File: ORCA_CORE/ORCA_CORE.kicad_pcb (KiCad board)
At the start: 4 copper layers, 73 x 134.1 mm, 184 parts, among them J1 data_line_power, J10 Raspberry_Pi_2_3, J11 I2C, J12 I2C, J13 6Vout, J15 Conn_01x05_Pin, J16 Conn_01x05_Pin, J17 Vin_motor, J18 data_line_power, J19 +5Vin_cpu, J2 I2C_power, J20 5Vout, J21 Conn_01x02, J3 Vout_motor, J4 emergence, J5 Vin_batt, J6 Vin_ex, J7 Vout_power2usp, J8 Vin_power2usp, J9 +5Vout_cpu, P1 USB_C_Receptacle_USB2.0, Q1 TJ60S04M3L, Q2 BSS138, Q3 BSS138, Q4 IRLML6402, Q5 TJ60S04M3L, Q6 BSS138, Q7 BSS138, Q8 BSS138, U1 LTC2301IMS, U10 HY2112, U11 AP64502, U12 TPS61230A__board, U13 FT230XS, U14 BNO055, U15 NJM78055DL1, U2 NJM78055DL1, U3 CN3058E, U4 RH1B-UDC6V, U5 TPH11006NL, U6 TPH11006NL, U7 NJW4860, U8 AZ1117-3.3, U9 FS8205

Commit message: placed an order
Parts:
- J21: footprint Battery:BatteryHolder_1xAA_code -> battery_case:BatteryHolder_1xAA_code
- R19: value 10 -> 360
- U12: footprint Converter_DCDC:TPS61230A -> converter_module:TPS61230A
- U4: footprint Relay_THT:RH1-U -> relay:RH1-U
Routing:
- net GND2: vias 49 -> 48

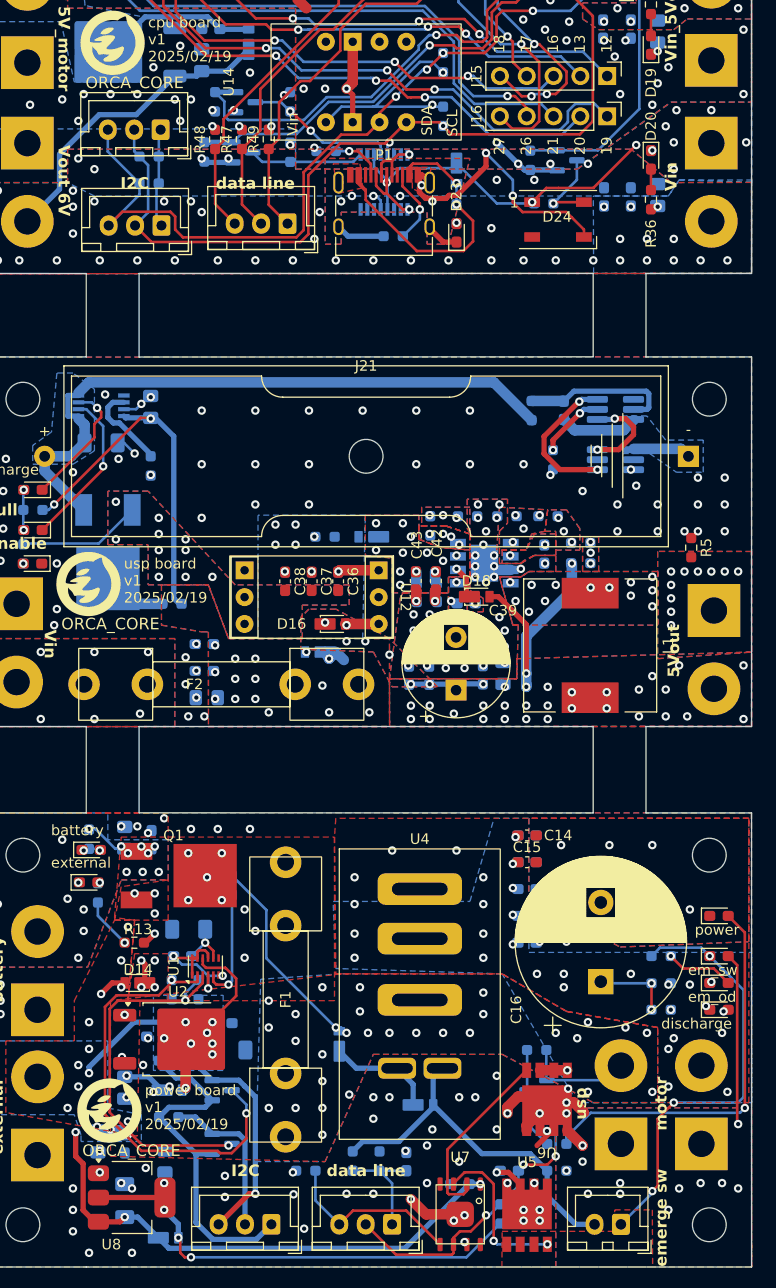
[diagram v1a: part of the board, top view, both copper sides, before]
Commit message: delete blind vias
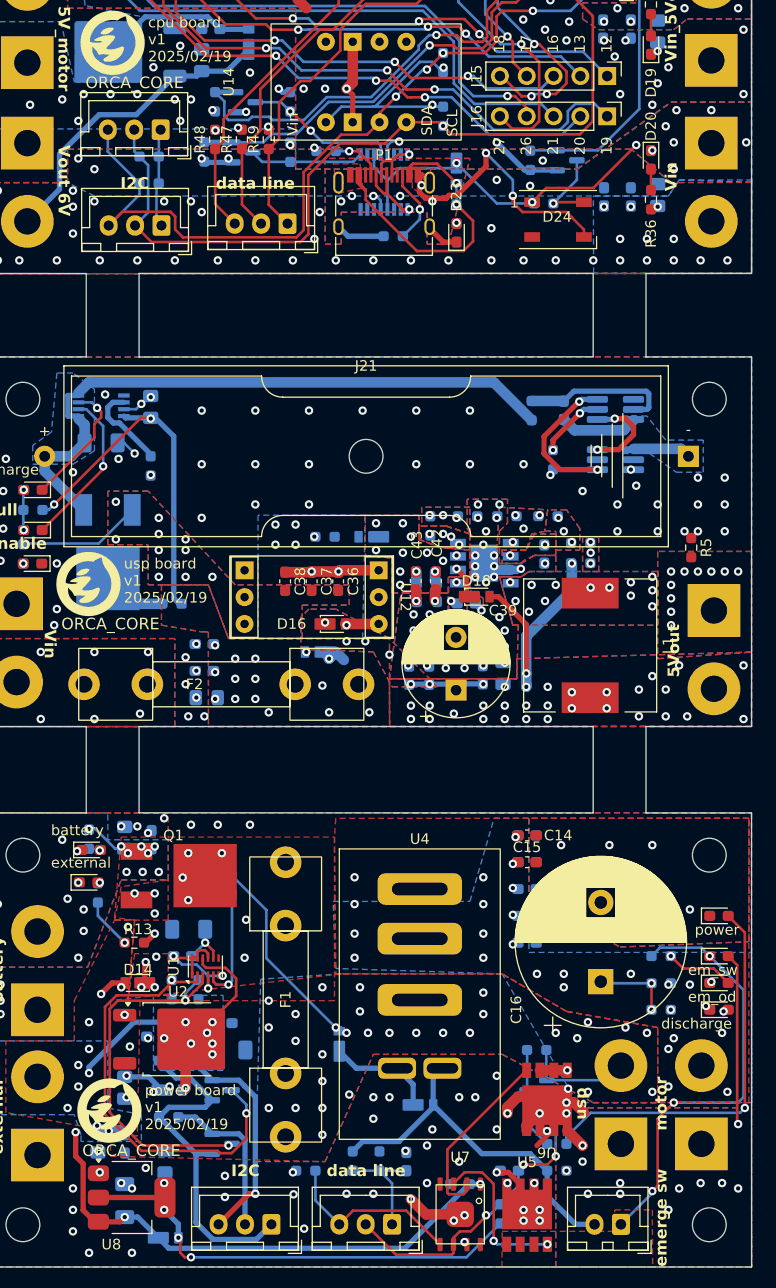
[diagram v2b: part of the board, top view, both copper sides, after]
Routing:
- net +5V_cpu: track 57.6 -> 64.6 mm
- net GND: track 73.9 -> 79.0 mm, vias 211 -> 206
- net Net-(U11-SW): track 4.14 -> 5.44 mm
- net +3V3_cpu: track 61.8 -> 62.8 mm
- net GND2: track 146.4 -> 147.3 mm
- net Net-(Q1-G): vias 6 -> 5
- net /power/Vout_motor: vias 27 -> 25
- net +VDD_power: vias 14 -> 12
- net +6V_cpu: vias 46 -> 44

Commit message: made board outline and import it
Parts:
- removed C13, C14, C15, C18, C22, C26, C28, C31, C32, C36, C37, C38, C40, C41, C42, C43, C46, C47, C51: 4.7u, Capacitor_SMD:C_0603_1608Metric_Pad1.08x0.95mm_HandSolder
- removed C16: 4700u, Capacitor_THT:CP_Radial_D16.0mm_P7.50mm
- removed C17, C30, C34, C35, C45: 0.1u, Capacitor_SMD:C_0603_1608Metric_Pad1.08x0.95mm_HandSolder
- removed C19: 10u/50V, Capacitor_SMD:C_1206_3216Metric_Pad1.33x1.80mm_HandSolder
- removed C20: 22u25V, Capacitor_SMD:C_0805_2012Metric_Pad1.18x1.45mm_HandSolder
- removed C21, C23, C24, C27, C33, C44, C48: 1u, Capacitor_SMD:C_0805_2012Metric_Pad1.18x1.45mm_HandSolder
- removed C25: 10u, Capacitor_SMD:C_1206_3216Metric_Pad1.33x1.80mm_HandSolder
- removed C29: 0.01u, Capacitor_SMD:C_0603_1608Metric_Pad1.08x0.95mm_HandSolder
- removed C39: 1000u, Capacitor_THT:CP_Radial_D10.0mm_P5.00mm
- removed C49: 1u/50V, Capacitor_SMD:C_0805_2012Metric_Pad1.18x1.45mm_HandSolder
- removed C50: 0.1u25V, Capacitor_SMD:C_0603_1608Metric_Pad1.08x0.95mm_HandSolder
- removed D10: LED_charge, LED_SMD:LED_0603_1608Metric_Pad1.05x0.95mm_HandSolder
- removed D11, D13, D14, D16, D17, D18, D22, D25, D9: CUHS20560, Diode:Diode_US2H
- removed D12: LED_full, LED_SMD:LED_0603_1608Metric_Pad1.05x0.95mm_HandSolder
- removed D15: LED_batt_enabled, LED_SMD:LED_0603_1608Metric_Pad1.05x0.95mm_HandSolder
- removed D20: LED_motor, LED_SMD:LED_0603_1608Metric_Pad1.05x0.95mm_HandSolder
- removed D23: LED_usb, LED_SMD:LED_0603_1608Metric_Pad1.05x0.95mm_HandSolder
- removed D24: WS2812B, LED_SMD:LED_WS2812B_PLCC4_5.0x5.0mm_P3.2mm
- removed F1, F2: Fuse, fuse:fuse
- removed L1: 10u, inductor:L_12x12mm_H8mm_withmodel
- removed ORCA_CORE (x3): LOGO, Logo:ORCA_logo
- removed Q4: IRLML6402, Package_TO_SOT_SMD:SOT-23
- removed Q5: TJ60S04M3L, toshiba:2-7M1A
- removed Q6, Q7: BSS138, Package_TO_SOT_SMD:SOT-23
- added H11: Hole_Vhub, MountingHole:MountingHole_3.2mm_M3, F.Cu at (-50.1, -137.2)
- added H12: Hole_Vhub, MountingHole:MountingHole_3.2mm_M3, F.Cu at (-42.1, -153.1)
- added H13: Hole_md, MountingHole:MountingHole_3.2mm_M3, F.Cu at (-92.0, 196.2)
- added H14: Hole_md, MountingHole:MountingHole_3.2mm_M3, F.Cu at (-92.0, 204.2)
- added H15: Hole_md, MountingHole:MountingHole_3.2mm_M3, F.Cu at (105.4, 71.9)
- added H16: Hole_md, MountingHole:MountingHole_3.2mm_M3, F.Cu at (105.4, 97.4)
- added H17: Hole_hat, MountingHole:MountingHole_3.2mm_M3, F.Cu at (162.0, -92.0)
- added H18: Hole_hat, MountingHole:MountingHole_3.2mm_M3, F.Cu at (162.0, -84.0)
- added H19: Hole_hat, MountingHole:MountingHole_3.2mm_M3, F.Cu at (162.0, -76.1)
- added H20: Hole_hat, MountingHole:MountingHole_3.2mm_M3, F.Cu at (162.0, -68.2)
- added H21: Hole_cpu, MountingHole:MountingHole_3.2mm_M3, F.Cu at (-307.2, -27.6)
- added H22: Hole_cup, MountingHole:MountingHole_3.2mm_M3, F.Cu at (-307.2, -19.7)
- added H23: Hole_usbA, MountingHole:MountingHole_3.2mm_M3, F.Cu at (-42.1, -145.2)
- added H24: Hole_usbA, MountingHole:MountingHole_3.2mm_M3, F.Cu at (-42.1, -137.2)
- added H7: Hole_Vext, MountingHole:MountingHole_3.2mm_M3, F.Cu at (-50.1, -153.1)
- added H8: Hole_Vext, MountingHole:MountingHole_3.2mm_M3, F.Cu at (-50.1, -145.2)
- added J14: limit_sw_upper, Connector_JST:JST_XH_S2B-XH-A_1x02_P2.50mm_Horizontal, F.Cu at (-87.4, 182.0)
- added J22: Vin_motor, Connector_JST:JST_XH_S2B-XH-A_1x02_P2.50mm_Horizontal, F.Cu at (127.0, 75.5)
- added J23: md_arm, Connector_JST:JST_XH_B6B-XH-A_1x06_P2.50mm_Vertical, F.Cu at (48.5, -92.6)
- added J24: md_fork, Connector_JST:JST_XH_B6B-XH-A_1x06_P2.50mm_Vertical, F.Cu at (48.5, -84.8)
- added J25: servo_arm, Connector_JST:JST_XH_B6B-XH-A_1x06_P2.50mm_Vertical, F.Cu at (48.5, -77.0)
- added J26: Vin_motor, Connector_JST:JST_XH_S2B-XH-A_1x02_P2.50mm_Horizontal, F.Cu at (-90.0, 1.64)
- added J27: servo_0, Connector_PinHeader_2.54mm:PinHeader_1x03_P2.54mm_Horizontal, F.Cu at (-114.2, -16.9)
- added J28: servo_1, Connector_PinHeader_2.54mm:PinHeader_1x03_P2.54mm_Horizontal, F.Cu at (-114.2, -7.23)
- added J29: servo_2, Connector_PinHeader_2.54mm:PinHeader_1x03_P2.54mm_Horizontal, F.Cu at (-114.2, 2.47)
- added J30: servo_3, Connector_PinHeader_2.54mm:PinHeader_1x03_P2.54mm_Horizontal, F.Cu at (-114.2, 12.2)
- added J31: I2C_1, Connector_JST:JST_XH_B3B-XH-A_1x03_P2.50mm_Vertical, F.Cu at (169.4, -84.8)
- added J32: I2C_2, Connector_JST:JST_XH_B3B-XH-A_1x03_P2.50mm_Vertical, F.Cu at (169.4, -77.0)
- added J33: cpu_male_2, Connector_PinHeader_2.54mm:PinHeader_2x05_P2.54mm_Vertical, F.Cu at (-305.4, -91.1)
- added J34: cpu_male_1, Connector_PinHeader_2.54mm:PinHeader_2x10_P2.54mm_Vertical, F.Cu at (-290.9, -118.2)
- added J35: hat_female_1, Connector_PinHeader_2.54mm:PinHeader_2x10_P2.54mm_Vertical, F.Cu at (88.5, -78.0)
- added J36: enable_arm, Connector_JST:JST_XH_S2B-XH-A_1x02_P2.50mm_Horizontal, F.Cu at (-134.0, -26.0)
- added J37: enable_arm, Connector_JST:JST_XH_B2B-XH-A_1x02_P2.50mm_Vertical, F.Cu at (82.4, -92.6)
- added J38: servo_arm, Connector_JST:JST_XH_S6B-XH-A_1x06_P2.50mm_Horizontal, F.Cu at (-144.0, -4.00)
- added J39: md_arm, Connector_JST:JST_XH_S6B-XH-A_1x06_P2.50mm_Horizontal, F.Cu at (110.5, 78.3)
- added J40: md_fork, Connector_JST:JST_XH_S6B-XH-A_1x06_P2.50mm_Horizontal, F.Cu at (-125.0, 187.0)
- added J41: cpu_female_2, Connector_PinHeader_2.54mm:PinHeader_2x05_P2.54mm_Vertical, F.Cu at (74.0, -51.0)
- added J42: uart, Connector_JST:JST_XH_B4B-XH-A_1x04_P2.50mm_Vertical, F.Cu at (68.0, -92.6)
- added J43: uart_device, Connector_JST:JST_XH_S4B-XH-A_1x04_P2.50mm_Horizontal, F.Cu at (-109.3, -138.2)
- added J44: servo_camera, Connector_PinHeader_2.54mm:PinHeader_1x03_P2.54mm_Vertical, F.Cu at (-282.0, -26.1)
- added J45: reset, Connector_JST:JST_XH_S3B-XH-A_1x03_P2.50mm_Horizontal, F.Cu at (-80.8, -110.7)
- added J46: reset, Connector_JST:JST_XH_B3B-XH-A_1x03_P2.50mm_Vertical, F.Cu at (96.8, -77.0)
- added J47: led, Connector_JST:JST_XH_B3B-XH-A_1x03_P2.50mm_Vertical, F.Cu at (96.8, -69.2)
- added J48: led, Connector_JST:JST_XH_B3B-XH-A_1x03_P2.50mm_Vertical, F.Cu at (-80.4, -122.5)
- added J49: USB_B_Micro, digikey-footprints:USB_Micro_B_Male_UJ2-MIBH-4-SMT-TR, F.Cu at (169.6, -67.6)
- added J50: USB_A, Connector_USB:USB_A_Kycon_KUSBX-AS1N-B_Horizontal, F.Cu at (-34.2, -130.7)
- added J51: usb_A_device, Connector_JST:JST_XH_S4B-XH-A_1x04_P2.50mm_Horizontal, F.Cu at (-109.3, -124.6)
- added J52: usb_A, Connector_JST:JST_XH_B4B-XH-A_1x04_P2.50mm_Vertical, F.Cu at (68.0, -84.8)
- added R52: 100, Resistor_SMD:R_0603_1608Metric_Pad0.98x0.95mm_HandSolder, F.Cu at (-304.7, -61.3)
- added R53: 2.2k, Resistor_SMD:R_0603_1608Metric_Pad0.98x0.95mm_HandSolder, F.Cu at (-304.7, -58.8)
- added R54: 2.2k, Resistor_SMD:R_0603_1608Metric_Pad0.98x0.95mm_HandSolder, F.Cu at (-304.7, -56.3)
- added R55: 100, Resistor_SMD:R_0603_1608Metric_Pad0.98x0.95mm_HandSolder, F.Cu at (-304.7, -53.8)
- added R56: 2.2k, Resistor_SMD:R_0603_1608Metric_Pad0.98x0.95mm_HandSolder, F.Cu at (-304.7, -51.3)
- added R57: 2.2k, Resistor_SMD:R_0603_1608Metric_Pad0.98x0.95mm_HandSolder, F.Cu at (180.1, -89.7)
- added R58: 2.2k, Resistor_SMD:R_0603_1608Metric_Pad0.98x0.95mm_HandSolder, F.Cu at (180.1, -87.2)
- added R59: 100, Resistor_SMD:R_0603_1608Metric_Pad0.98x0.95mm_HandSolder, F.Cu at (-304.7, -48.8)
- added R60: 2.2k, Resistor_SMD:R_0603_1608Metric_Pad0.98x0.95mm_HandSolder, F.Cu at (-300.4, -68.8)
- added R61: 2.2k, Resistor_SMD:R_0603_1608Metric_Pad0.98x0.95mm_HandSolder, F.Cu at (-300.4, -66.3)
- added R62: 100, Resistor_SMD:R_0603_1608Metric_Pad0.98x0.95mm_HandSolder, F.Cu at (-300.4, -63.8)
- added R63: 2.2k, Resistor_SMD:R_0603_1608Metric_Pad0.98x0.95mm_HandSolder, F.Cu at (-300.4, -61.3)
- added R64: 2.2k, Resistor_SMD:R_0603_1608Metric_Pad0.98x0.95mm_HandSolder, F.Cu at (-300.4, -58.8)
- added R65: 100, Resistor_SMD:R_0603_1608Metric_Pad0.98x0.95mm_HandSolder, F.Cu at (-300.4, -56.3)
- added R66: 2.2k, Resistor_SMD:R_0603_1608Metric_Pad0.98x0.95mm_HandSolder, F.Cu at (-300.4, -53.8)
- added R67: 2.2k, Resistor_SMD:R_0603_1608Metric_Pad0.98x0.95mm_HandSolder, F.Cu at (-300.4, -51.3)
- added R68: 100, Resistor_SMD:R_0603_1608Metric_Pad0.98x0.95mm_HandSolder, F.Cu at (-300.4, -48.8)
- added R69: 2.2k, Resistor_SMD:R_0603_1608Metric_Pad0.98x0.95mm_HandSolder, F.Cu at (-296.0, -68.8)
- added R70: 2.2k, Resistor_SMD:R_0603_1608Metric_Pad0.98x0.95mm_HandSolder, F.Cu at (-296.0, -66.3)
- added R71: 2.2k, Resistor_SMD:R_0603_1608Metric_Pad0.98x0.95mm_HandSolder, F.Cu at (-296.0, -63.8)
- added R72: 2.2k, Resistor_SMD:R_0603_1608Metric_Pad0.98x0.95mm_HandSolder, F.Cu at (-296.0, -61.3)
- added R73: 2.2k, Resistor_SMD:R_0603_1608Metric_Pad0.98x0.95mm_HandSolder, F.Cu at (-296.0, -58.8)
- added SW2: REST_sw, Button_Switch_THT:SW_PUSH_6mm, F.Cu at (-36.1, -145.1)
- added U16: TLP293, Package_SO:SOIC-4_4.55x2.6mm_P1.27mm, F.Cu at (-98.3, 17.0)
- added U17: AZ1117-3.3, Package_TO_SOT_SMD:SOT-223-3_TabPin2, F.Cu at (-88.5, 16.1)
- added U18: TLP293, Package_SO:SOIC-4_4.55x2.6mm_P1.27mm, F.Cu at (-298.4, -45.4)
- added U19: TLP293, Package_SO:SOIC-4_4.55x2.6mm_P1.27mm, F.Cu at (-298.4, -41.3)
- added U20: TLP293, Package_SO:SOIC-4_4.55x2.6mm_P1.27mm, F.Cu at (-298.4, -37.1)
- added U21: TLP293, Package_SO:SOIC-4_4.55x2.6mm_P1.27mm, F.Cu at (-298.4, -33.0)
- added U22: AZ1117-3.3, Package_TO_SOT_SMD:SOT-223-3_TabPin2, F.Cu at (-277.6, -56.2)
- added U23: TLP293, Package_SO:SOIC-4_4.55x2.6mm_P1.27mm, F.Cu at (-298.4, -28.8)
- added U24: TLP293, Package_SO:SOIC-4_4.55x2.6mm_P1.27mm, F.Cu at (-298.4, -24.7)
- added U25: TLP293, Package_SO:SOIC-4_4.55x2.6mm_P1.27mm, F.Cu at (-298.4, -20.5)
- C1: value 1u/50V -> 10u/50V; footprint Capacitor_SMD:C_0805_2012Metric_Pad1.18x1.45mm_HandSolder -> Capacitor_SMD:C_1206_3216Metric_Pad1.33x1.80mm_HandSolder; moved to F.Cu
- C10, C12: value 4.7u -> 22u25V; footprint Capacitor_SMD:C_0603_1608Metric_Pad1.08x0.95mm_HandSolder -> Capacitor_SMD:C_0805_2012Metric_Pad1.18x1.45mm_HandSolder; moved to F.Cu
- C11, C9: value 4.7u -> 10u/50V; footprint Capacitor_SMD:C_0603_1608Metric_Pad1.08x0.95mm_HandSolder -> Capacitor_SMD:C_1206_3216Metric_Pad1.33x1.80mm_HandSolder; moved to F.Cu
- C2: value 0.1u25V -> 22u25V; footprint Capacitor_SMD:C_0603_1608Metric_Pad1.08x0.95mm_HandSolder -> Capacitor_SMD:C_0805_2012Metric_Pad1.18x1.45mm_HandSolder; moved to F.Cu
- C3: value 0.1u -> 10u/50V; footprint Capacitor_SMD:C_0603_1608Metric_Pad1.08x0.95mm_HandSolder -> Capacitor_SMD:C_1206_3216Metric_Pad1.33x1.80mm_HandSolder
- C4: value 4.7u -> 22u25V; footprint Capacitor_SMD:C_0603_1608Metric_Pad1.08x0.95mm_HandSolder -> Capacitor_SMD:C_0805_2012Metric_Pad1.18x1.45mm_HandSolder
- C5: value 10u -> 0.1u; footprint Capacitor_SMD:C_1206_3216Metric_Pad1.33x1.80mm_HandSolder -> Capacitor_SMD:C_0603_1608Metric_Pad1.08x0.95mm_HandSolder; moved to F.Cu
- C6, Q2, Q8, R12, R34, R37, R38, R41, R43, R44, R46, R50, R6, R7, R8: moved to F.Cu
- C7: value 10u -> 220u; moved to F.Cu
- C8: value 0.1u -> 220u; footprint Capacitor_SMD:C_0603_1608Metric_Pad1.08x0.95mm_HandSolder -> Capacitor_SMD:C_1206_3216Metric_Pad1.33x1.80mm_HandSolder; moved to F.Cu
- D1: value LED_batt -> CUHS20560; footprint LED_SMD:LED_0603_1608Metric_Pad1.05x0.95mm_HandSolder -> Diode:Diode_US2H
- D19: value LED_cpu -> pwr_cpu
- D2: value LED_ex -> CUHS20560; footprint LED_SMD:LED_0603_1608Metric_Pad1.05x0.95mm_HandSolder -> Diode:Diode_US2H; moved to B.Cu
- D3: value CUHS20560 -> WS2812B; footprint Diode:Diode_US2H -> LED_SMD:LED_WS2812B_PLCC4_5.0x5.0mm_P3.2mm; moved to F.Cu
- D4: value CUHS20560 -> enable_arm; footprint Diode:Diode_US2H -> LED_SMD:LED_0603_1608Metric_Pad1.05x0.95mm_HandSolder; moved to F.Cu
- D5: value LED_power -> power_input_arm
- D6: value LED_emerge_switch -> CUHS20560; footprint LED_SMD:LED_0603_1608Metric_Pad1.05x0.95mm_HandSolder -> Diode:Diode_US2H
- D7: value LED_emerge_order -> CUHS20560; footprint LED_SMD:LED_0603_1608Metric_Pad1.05x0.95mm_HandSolder -> Diode:Diode_US2H
- D8: value LED_discharge -> pwr_motor
- H1, H2: value Hole_power -> Hole_uart
- H3, H4: value Hole_power -> Hole_led
- H5, H6: value Hole_usp -> Hole_reset
- J1: value data_line_power -> Vext_in; footprint Connector_JST:JST_XH_B3B-XH-A_1x03_P2.50mm_Vertical -> Conn:AMASS_XT60_Vertifcal_withmodel_female
- J11: value I2C -> wheel_left; footprint Connector_JST:JST_XH_B3B-XH-A_1x03_P2.50mm_Vertical -> Connector_PinHeader_2.54mm:PinHeader_1x03_P2.54mm_Vertical
- J12: value I2C -> md_out; footprint Connector_JST:JST_XH_B3B-XH-A_1x03_P2.50mm_Vertical -> Connector_JST:JST_XH_S2B-XH-A_1x02_P2.50mm_Horizontal
- J13: value 6Vout -> md_out; footprint Conn:power_pad -> Connector_JST:JST_XH_S2B-XH-A_1x02_P2.50mm_Horizontal
- J15: value Conn_01x05_Pin -> limit_sw_upper; footprint Connector_PinHeader_2.54mm:PinHeader_1x05_P2.54mm_Vertical -> Connector_JST:JST_XH_S2B-XH-A_1x02_P2.50mm_Horizontal
- J16: value Conn_01x05_Pin -> limit_sw_under; footprint Connector_PinHeader_2.54mm:PinHeader_1x05_P2.54mm_Vertical -> Connector_JST:JST_XH_S2B-XH-A_1x02_P2.50mm_Horizontal
- J17: value Vin_motor -> data_line_power; footprint Conn:power_pad -> Connector_JST:JST_XH_B3B-XH-A_1x03_P2.50mm_Vertical
- J18: value data_line_power -> +6V_motor; footprint Connector_JST:JST_XH_B3B-XH-A_1x03_P2.50mm_Vertical -> Conn:power_pad
- J2: value I2C_power -> 6Vout; footprint Connector_JST:JST_XH_B3B-XH-A_1x03_P2.50mm_Vertical -> Conn:AMASS_XT30U-F_Vertical_withmodel_male
- J20: value 5Vout -> limit_sw_under; footprint Conn:power_pad -> Connector_JST:JST_XH_S2B-XH-A_1x02_P2.50mm_Horizontal
- J21: value Conn_01x02 -> Vin_motor; footprint battery_case:BatteryHolder_1xAA_code -> Connector_JST:JST_XH_S2B-XH-A_1x02_P2.50mm_Horizontal
- J3: value Vout_motor -> 6Vout; footprint Conn:power_pad -> Conn:AMASS_XT30U-F_Vertical_withmodel_male
- J4: value emergence -> 6Vout; footprint Connector_JST:JST_XH_B2B-XH-A_1x02_P2.50mm_Vertical -> Conn:AMASS_XT30U-F_Vertical_withmodel_male
- J5: value Vin_batt -> 6Vin; footprint Conn:power_pad -> Conn:AMASS_XT60_Vertifcal_withmodel_female
- J6: value Vin_ex -> Vext_out
- J7: value Vout_power2usp -> 6Vout; footprint Conn:power_pad -> Conn:AMASS_XT30U-F_Vertical_withmodel_male
- J8: value Vin_power2usp -> wheel_front; footprint Conn:power_pad -> Connector_PinHeader_2.54mm:PinHeader_1x03_P2.54mm_Horizontal
- J9: value +5Vout_cpu -> wheel_right; footprint Conn:power_pad -> Connector_PinHeader_2.54mm:PinHeader_1x03_P2.54mm_Vertical
- Q1: value TJ60S04M3L -> BSS138; footprint toshiba:2-7M1A -> Package_TO_SOT_SMD:SOT-23
- Q3: value BSS138 -> TJ60S04M3L; footprint Package_TO_SOT_SMD:SOT-23 -> toshiba:2-7M1A; moved to F.Cu
- R1: value 1k -> 560; moved to F.Cu
- R10, R42, R45: value 2.2k -> 100; moved to F.Cu
- R11: value 2.2k -> 100
- R13: value 4.7k -> 2.2k; moved to B.Cu
- R14, R17, R18, R20, R22, R40: value 1k -> 2.2k; moved to F.Cu
- R15, R4: value 4.7k -> 2.2k; moved to F.Cu
- R16: value 4.7k -> 100; moved to F.Cu
- R19: value 360 -> 100
- R2: value 1k -> 5.1k; moved to F.Cu
- R21: value 1.2k -> 2.2k
- R23: value 100k -> 2.2k
- R24: value 100k -> 2.2k; moved to F.Cu
- R25: value 47k -> 2.2k
- R26: value 4.7k -> 10k; moved to F.Cu
- R27: value 510 -> 1k; moved to F.Cu
- R28: value 10k -> 1k; moved to F.Cu
- R29: value 2k -> 100; moved to F.Cu
- R3: value 4.7k -> 5.1k; moved to F.Cu
- R30: value 100 -> 2.2k; moved to F.Cu
- R31: value 1k -> 47; moved to F.Cu
- R32: value 10k -> 100; moved to F.Cu
- R33: value 10k -> 2.2k; moved to F.Cu
- R36: value 1k -> 2.2k
- R39, R51: value 5.1k -> 100; moved to F.Cu
- R49: value 2.2k -> 1k
- R5: value 0 -> 2.2k
- R9: value 2.2k -> 10k; moved to F.Cu
- U1: value LTC2301IMS -> FT230XS; footprint Package_DFN_QFN:TDFN-12_2x3mm_P0.5mm -> Package_SO:SSOP-16_3.9x4.9mm_P0.635mm
- U10: value HY2112 -> TLP293; footprint Package_TO_SOT_SMD:TSOT-23-6_HandSoldering -> Package_SO:SOIC-4_4.55x2.6mm_P1.27mm; moved to F.Cu
- U11: value AP64502 -> TLP293; footprint Package_SO:Diodes_SO-8EP -> Package_SO:SOIC-4_4.55x2.6mm_P1.27mm; moved to F.Cu
- U12: value TPS61230A__board -> TLP293; footprint converter_module:TPS61230A -> Package_SO:SOIC-4_4.55x2.6mm_P1.27mm
- U13: value FT230XS -> TLP293; footprint Package_SO:SSOP-16_3.9x4.9mm_P0.635mm -> Package_SO:SOIC-4_4.55x2.6mm_P1.27mm; moved to F.Cu
- U15: value NJM78055DL1 -> TLP293; footprint Package_TO_SOT_SMD:TO-252-2 -> Package_SO:SOIC-4_4.55x2.6mm_P1.27mm; moved to F.Cu
- U2: value NJM78055DL1 -> PCA9685PW_Q900_118; footprint Package_TO_SOT_SMD:TO-252-2 -> digikey-footprints:TSSOP-28_W4.40mm
- U3: value CN3058E -> AM2837; footprint Package_SO:TSSOP-8_3x3mm_P0.65mm -> Package_SO:SOP-8_3.9x4.9mm_P1.27mm; moved to F.Cu
- U4: value RH1B-UDC6V -> AM2837; footprint relay:RH1-U -> Package_SO:SOP-8_3.9x4.9mm_P1.27mm; moved to B.Cu
- U5, U6: value TPH11006NL -> TLP293; footprint toshiba:2-5Q1S -> Package_SO:SOIC-4_4.55x2.6mm_P1.27mm
- U7: value NJW4860 -> AZ1117-3.3; footprint nisshinbo:TSOP8-M1 -> Package_TO_SOT_SMD:SOT-223-3_TabPin2
- U8: moved to B.Cu
- U9: value FS8205 -> TLP293; footprint Package_TO_SOT_SMD:TSOT-23-6_HandSoldering -> Package_SO:SOIC-4_4.55x2.6mm_P1.27mm; moved to F.Cu
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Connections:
- net full_color_led_5V renamed /cpu/led
- C1 pad 1: +6V_power -> +6V
- C10 pad 1: /power/Vout_motor -> +3V3
- C11 pad 1: /power/Vout_motor -> +6V
- C12 pad 1: /power/Vout_motor -> +3V3_motor
- C2 pad 1: +5V_power -> +3V3
- C3 pad 1: /power/power_checker -> +6V
- C4 pad 1: GND -> +3V3
- C4 pad 2: +VDD_power -> GND
- C5 pad 1: GND -> +6V
- C5 pad 2: Net-(U1-REFCOMP) -> GND
- C6 pad 1: GND -> +6V
- C6 pad 2: Net-(U1-REFCOMP) -> GND
- C7 pad 1: +5V_power -> +6V
- C8 pad 1: +5V_power -> +6V
- C9 pad 1: /power/Vout_motor -> +6V_in
- D1 pad 1: GND -> +6V
- D1 pad 2: Net-(D1-A) -> +3V3
- D19 pad 1: GND2 -> GND1
- D2 pad 1: GND -> +6V
- D2 pad 2: Net-(D2-A) -> +3V3
- D3 pad 1: Net-(D3-K) -> /external_io/+5V_led
- D3 pad 2: +6V_power -> unconnected-(D3-DOUT-Pad2)
- D4 pad 1: Net-(D3-K) -> GND
- D6 pad 1: Net-(D6-K) -> +6V_in
- D6 pad 2: Net-(D6-A) -> +3V3
- D7 pad 1: GND -> +6V
- D7 pad 2: Net-(D7-A) -> +3V3_motor
- D8 pad 1: Net-(D8-K) -> GND
- J1 pad 1: /power/emerg_detector -> Net-(J1-Pin_1)
- J1 pad 2: /power/power_checker -> Net-(J1-Pin_2)
- J10 pad 1: +3V3_cpu -> +3V3
- J10 pad 13: /cpu/GPIO27 -> unconnected-(J10-GPIO27-Pad13)
- J10 pad 14: GND2 -> GND1
- J10 pad 15: /cpu/emerg_detector -> emerge_detector
- J10 pad 16: /cpu/emerge_order -> power_checker
- J10 pad 17: +3V3_cpu -> +3V3
- J10 pad 18: /cpu/power_checker -> emerge_order
- J10 pad 2: +5V_cpu -> +5V
- J10 pad 20: GND2 -> GND1
- J10 pad 25: GND2 -> GND1
- J10 pad 3: SDA -> /cpu/SDA_cpu
- J10 pad 30: GND2 -> GND1
- J10 pad 34: GND2 -> GND1
- J10 pad 35: /cpu/GPIO19 -> /cpu/rest
- J10 pad 37: /cpu/GPIO26 -> unconnected-(J10-GPIO26-Pad37)
- J10 pad 38: /cpu/GPIO20 -> unconnected-(J10-GPIO20/MOSI1-Pad38)
- J10 pad 39: GND2 -> GND1
- J10 pad 4: +5V_cpu -> +5V
- J10 pad 40: /cpu/GPIO21 -> unconnected-(J10-GPIO21/SCLK1-Pad40)
- J10 pad 5: SCL -> /cpu/SCL_cpu
- J10 pad 6: GND2 -> GND1
- J10 pad 9: GND2 -> GND1
- J11 pad 1: +3V3_cpu -> GND
- J11 pad 2: SCL -> +6V
- J11 pad 3: SDA -> Net-(J11-Pin_3)
- J12 pad 1: +3V3_cpu -> Net-(J12-Pin_1)
- J12 pad 2: SCL -> Net-(J12-Pin_2)
- J13 pad 1: GND -> Net-(J13-Pin_1)
- J13 pad 2: +6V_cpu -> Net-(J13-Pin_2)
- J15 pad 1: /cpu/GPIO12 -> GND1
- J15 pad 2: /cpu/GPIO13 -> /md_arm/limit_sw_upper
- J16 pad 1: /cpu/GPIO19 -> GND1
- J16 pad 2: /cpu/GPIO20 -> /md_fork/limit_sw_under
- J17 pad 1: GND -> /cpu_hat/emerge_detector
- J17 pad 2: +6V_cpu -> /cpu_hat/power_checker
- J18 pad 1: /cpu/emerg_detector -> GND
- J18 pad 2: /cpu/power_checker -> +6V
- J19 pad 1: GND2 -> GND1
- J19 pad 2: +5V_cpu -> +5V
- J2 pad 1: VBUS_power -> Net-(J2-Pin_1)
- J2 pad 2: /power/SCL_3V3 -> Net-(J2-Pin_2)
- J20 pad 1: GND -> GND1
- J20 pad 2: +5V_cpu2servo -> /md_arm/limit_sw_under
- J21 pad 1: batt- -> GND
- J21 pad 2: batt+ -> +6V
- J3 pad 1: GND -> Net-(J2-Pin_1)
- J3 pad 2: /power/Vout_motor -> Net-(J2-Pin_2)
- J4 pad 1: Net-(D6-K) -> Net-(J2-Pin_1)
- J4 pad 2: Net-(D4-A) -> Net-(J2-Pin_2)
- J5 pad 1: GND -> Net-(J2-Pin_1)
- J5 pad 2: +BATT_power -> Net-(J2-Pin_2)
- J6 pad 1: GND -> Net-(J1-Pin_1)
- J6 pad 2: +VDD_power -> Net-(J1-Pin_2)
- J7 pad 1: GND -> Net-(J2-Pin_1)
- J7 pad 2: +6V_power -> Net-(J2-Pin_2)
- J8 pad 2: /usp/Vin -> +6V
- J9 pad 1: GND1 -> GND
- J9 pad 2: reg_down_out -> +6V
- P1 pad A1: GND2 -> /external_io/GND_uart
- P1 pad A12: GND2 -> /external_io/GND_uart
- P1 pad A4: Net-(D22-A) -> /external_io/+5V_uart
- P1 pad A6: Net-(U13-USBDP) -> Net-(U1-USBDP)
- P1 pad A7: Net-(U13-USBDM) -> Net-(U1-USBDM)
- P1 pad A9: Net-(D22-A) -> /external_io/+5V_uart
- P1 pad B1: GND2 -> /external_io/GND_uart
- P1 pad B12: GND2 -> /external_io/GND_uart
- P1 pad B4: Net-(D22-A) -> /external_io/+5V_uart
- P1 pad B6: Net-(U13-USBDP) -> Net-(U1-USBDP)
- P1 pad B7: Net-(U13-USBDM) -> Net-(U1-USBDM)
- P1 pad B9: Net-(D22-A) -> /external_io/+5V_uart
- P1 pad S1: GND2 -> /external_io/GND_uart
- Q1 pad 1: +BATT_power -> +3V3
- Q1 pad 2: Net-(Q1-G) -> TXD_3V3
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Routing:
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- removed copper zone on In1.Cu, net +3V3_cpu
- removed copper zone on B.Cu, net +5V_cpu
- removed copper zone on F.Cu, net +5V_cpu
- removed copper zone on In1.Cu, net +5V_cpu
- removed copper zone on In2.Cu, net +5V_cpu
- removed copper zone on B.Cu, net +5V_cpu2servo
- removed copper zone on In1.Cu, net +5V_cpu2servo
- removed copper zone on B.Cu, net +5V_power
- removed copper zone on B.Cu, net +6V_cpu
- removed copper zone on F.Cu, net +6V_cpu
- removed copper zone on In1.Cu, net +6V_cpu
- removed copper zone on B.Cu, net +6V_power
- removed copper zone on F.Cu, net +6V_power
- removed copper zone on In1.Cu, net +6V_power
- removed copper zone on B.Cu, net +BATT_power
- removed copper zone on F.Cu, net +BATT_power
- removed copper zone on In1.Cu, net +BATT_power
- removed copper zone on B.Cu, net +VDD_power
- removed copper zone on F.Cu, net +VDD_power
- removed copper zone on In1.Cu, net +VDD_power
- removed copper zone on B.Cu, net +VDD_usp
- removed copper zone on F.Cu, net +VDD_usp
- removed copper zone on In1.Cu, net +VDD_usp
- removed copper zone on B.Cu, net /power/Vout_motor
- removed copper zone on F.Cu, net /power/Vout_motor
- removed copper zone on In1.Cu, net /power/Vout_motor
- removed copper zone on B.Cu, net /usp/Vin
- removed copper zone on F.Cu, net /usp/Vin
- removed copper zone on In1.Cu, net /usp/Vin
- removed copper zone on In2.Cu, net /usp/Vin
- removed copper zone on In1.Cu, net GND
- removed copper zone on In2.Cu, net GND
- removed copper zone on In1.Cu, net GND1
- removed copper zone on In2.Cu, net GND1
- removed copper zone on B.Cu, net GND2
- removed copper zone on F.Cu, net GND2
- removed copper zone on In2.Cu, net GND2
- removed copper zone on F.Cu, net Net-(D14-K)
- removed copper zone on In1.Cu, net Net-(D14-K)
- removed copper zone on F.Cu, net Net-(D6-K)
- removed copper zone on In2.Cu, net Net-(Q1-G)
- removed copper zone on B.Cu, net Net-(R23-Pad2)
- removed copper zone on F.Cu, net Net-(R23-Pad2)
- removed copper zone on In1.Cu, net Net-(R23-Pad2)
- removed copper zone on In2.Cu, net Net-(R23-Pad2)
- removed copper zone on B.Cu, net Net-(R25-Pad1)
- removed copper zone on F.Cu, net Net-(R25-Pad1)
- removed copper zone on In1.Cu, net Net-(R25-Pad1)
- removed copper zone on In2.Cu, net Net-(R25-Pad1)
- removed copper zone on B.Cu, net Net-(R26-Pad2)
- removed copper zone on F.Cu, net Net-(R26-Pad2)
- removed copper zone on In1.Cu, net Net-(R26-Pad2)
- removed copper zone on In2.Cu, net Net-(R26-Pad2)
- removed copper zone on B.Cu, net Net-(U11-BST)
- removed copper zone on F.Cu, net Net-(U11-BST)
- removed copper zone on In1.Cu, net Net-(U11-BST)
- removed copper zone on In2.Cu, net Net-(U11-BST)
- removed copper zone on B.Cu, net Net-(U11-FB)
- removed copper zone on F.Cu, net Net-(U11-FB)
- removed copper zone on In1.Cu, net Net-(U11-FB)
- removed copper zone on In2.Cu, net Net-(U11-FB)
- removed copper zone on B.Cu, net Net-(U11-RT/CLK)
- removed copper zone on F.Cu, net Net-(U11-RT/CLK)
- removed copper zone on In1.Cu, net Net-(U11-RT/CLK)
- removed copper zone on In2.Cu, net Net-(U11-RT/CLK)
- removed copper zone on B.Cu, net Net-(U11-SS)
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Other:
- board size 73 x 134.1 mm -> 123.1 x 120.2 mm
- copper layers 4 -> 2
- board text removed: "12"
- board text removed: "13"
- board text removed: "16"
- board text removed: "17"
- board text removed: "18"
- board text removed: "19"
- board text removed: "20"
- board text removed: "21"
- board text removed: "26"
- board text removed: "27"
- board text removed: "3V3"
- board text removed: "5Vout"
- board text removed: "I2C"
- board text removed: "SCL"
- board text removed: "SDA"
- board text removed: "Vin"
- board text removed: "Vin_5Vcpu"
- board text removed: "Vout 5V_motor"
- board text removed: "Vout 6V"
- board text removed: "battery"
- board text removed: "charge"
- board text removed: "cpu board v1 2025/02/19"
- board text removed: "data line"
- board text removed: "discharge"
- board text removed: "em_od"
- board text removed: "em_sw"
- board text removed: "emerge sw"
- board text removed: "emerge_detector"
- board text removed: "emerge_order"
- board text removed: "enable"
- board text removed: "external"
- board text removed: "full"
- board text removed: "motor"
- board text removed: "power"
- board text removed: "power board v1 2025/02/19"
- board text removed: "power_checker"
- board text removed: "usp"
- board text removed: "usp board v1 2025/02/19"

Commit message: place most of footprints. test replicate
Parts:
- removed R57, R58: 2.2k, Resistor_SMD:R_0603_1608Metric_Pad0.98x0.95mm_HandSolder
- added J53: cover_left, Connector_PinHeader_2.54mm:PinHeader_1x07_P2.54mm_Vertical, B.Cu at (173.7, 139.7)
- added J54: base_left, Connector_PinSocket_2.54mm:PinSocket_1x07_P2.54mm_Vertical, F.Cu at (147.5, 76.2)
- added J59: base_right, Connector_PinSocket_2.54mm:PinSocket_2x10_P2.54mm_Vertical, F.Cu at (52.5, 89.8)
- added J60: cover_right, Connector_PinHeader_2.54mm:PinHeader_2x10_P2.54mm_Vertical, B.Cu at (209.3, 139.7)
- J10: footprint cpu:raspberrypi_Zero_W_Vertical -> cpu:raspberrypi_Zerp_W_horisontal
- J27, J28, J29, J30: footprint Connector_PinHeader_2.54mm:PinHeader_1x03_P2.54mm_Horizontal -> Connector_PinHeader_2.54mm:PinHeader_1x03_P2.54mm_Vertical
- J33: value cpu_male_2 -> cpu_female_left; footprint Connector_PinHeader_2.54mm:PinHeader_2x05_P2.54mm_Vertical -> Connector_PinSocket_2.54mm:PinSocket_2x05_P2.54mm_Vertical
- J34: value cpu_male_1 -> cpu_female_right; footprint Connector_PinHeader_2.54mm:PinHeader_2x10_P2.54mm_Vertical -> Connector_PinSocket_2.54mm:PinSocket_2x10_P2.54mm_Vertical
- J35: value hat_female_1 -> hat_male_right; moved to B.Cu
- J41: value cpu_female_2 -> cpu_male_left; moved to B.Cu
- J44, J9: footprint Connector_PinHeader_2.54mm:PinHeader_1x03_P2.54mm_Vertical -> Connector_PinHeader_2.54mm:PinHeader_1x03_P2.54mm_Horizontal
- J45: footprint Connector_JST:JST_XH_S3B-XH-A_1x03_P2.50mm_Horizontal -> Connector_JST:JST_XH_B3B-XH-A_1x03_P2.50mm_Vertical; moved to B.Cu
- J48, Q1, Q2, R1, R2, R3, R37, R38, R4, R5, R7, R8, U1, U18, U19, U20: moved to B.Cu
- J49: footprint digikey-footprints:USB_Micro_B_Male_UJ2-MIBH-4-SMT-TR -> Conn:ZX60-B-5S(31); moved to B.Cu
- U14: footprint IMU:BNO055 -> IMU:BNO055_short
- moved J10 497.5 mm to (114.0, 132.9), turned to 180 degrees
- moved R34 470.1 mm to (139.7, 86.4), turned to 90 degrees
- moved R6 470.0 mm to (135.0, 90.2)
- moved J33 464.2 mm to (130.2, 69.3), turned to 30 degrees
- moved R69 458.5 mm to (133.1, 92.7)
- moved R48 455.2 mm to (108.3, 122.6), turned to 180 degrees
- moved R68 452.4 mm to (127.8, 97.3), turned to 60 degrees
- moved J18 451.0 mm to (103.8, 136.9)
- moved R70 450.0 mm to (123.7, 96.1), turned to -30 degrees
- moved R55 449.8 mm to (108.3, 124.5)
- moved R56 447.4 mm to (108.2, 120.9), turned to 180 degrees
- moved R51 447.0 mm to (100.7, 124.5)
- moved R9 446.4 mm to (106.1, 108.0)
- moved D7 445.2 mm to (106.7, 157.9)
- moved R53 443.3 mm to (100.6, 120.9), turned to 180 degrees
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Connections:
- J17 pad 1: /cpu_hat/emerge_detector -> Net-(J17-Pin_1)
- J17 pad 2: /cpu_hat/power_checker -> Net-(J17-Pin_2)
- J17 pad 3: /cpu_hat/emerge_order -> Net-(J17-Pin_3)
- J23 pad 2: /cpu_hat/IN_A_fork -> /cpu_hat/IN_A_arm_out
- J23 pad 3: /cpu_hat/IN_B_fork -> /cpu_hat/IN_B_arm_out
- J23 pad 4: /cpu_hat/limit_sw_upper_arm -> /cpu_hat/limit_sw_upper_arm_in
- J23 pad 5: /cpu_hat/limit_sw_under_arm -> /cpu_hat/limit_sw_under_arm_in
- J24 pad 2: /cpu_hat/IN_A_arm -> /cpu_hat/IN_A_fork_out
- J24 pad 3: /cpu_hat/IN_B_arm -> /cpu_hat/IN_B_fork_out
- J24 pad 4: /cpu_hat/limit_sw_upper_fork -> /cpu_hat/limit_sw_upper_fork_in
- J24 pad 5: /cpu_hat/limit_sw_under_fork -> /cpu_hat/limit_sw_under_fork_in
- J25 pad 2: /cpu_hat/servo_0 -> /cpu_hat/servo_0_out
- J25 pad 3: /cpu_hat/servo_1 -> /cpu_hat/servo_1_out
- J25 pad 4: /cpu_hat/servo_2 -> /cpu_hat/servo_2_out
- J25 pad 5: /cpu_hat/servo_3 -> /cpu_hat/servo_3_out
- J31 pad 2: /cpu_hat/SCL -> Net-(J31-Pin_2)
- J31 pad 3: /cpu_hat/SDA -> Net-(J31-Pin_3)
- J32 pad 2: /cpu_hat/SCL -> Net-(J31-Pin_2)
- J32 pad 3: /cpu_hat/SDA -> Net-(J31-Pin_3)
- J37 pad 2: /cpu_hat/enable_arm -> /cpu_hat/enable_arm_out
- J42 pad 2: /cpu_hat/TX -> /cpu_hat/TX_out
- J42 pad 3: /cpu_hat/RX -> /cpu_hat/RX_out
- J49 pad SH: (no net) -> /cpu_hat/GND_usb
- R37 pad 2: /cpu_hat/SDA -> Net-(J31-Pin_3)
- R38 pad 2: /cpu_hat/SCL -> Net-(J31-Pin_2)
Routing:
- net +3V3: track 29.2 -> 136.1 mm, vias 2 -> 6
- net +5V: track 0.00 -> 59.2 mm, vias 0 -> 2
- net Net-(J31-Pin_2): track 0.00 -> 52.3 mm, vias 0 -> 2
- net Net-(J31-Pin_3): track 0.00 -> 47.8 mm, vias 0 -> 1
- net Net-(J17-Pin_2): track 0.00 -> 45.4 mm
- net /cpu_hat/limit_sw_upper_fork_in: track 0.00 -> 42.0 mm
- net /cpu_hat/IN_A_fork_out: track 0.00 -> 39.8 mm, vias 0 -> 3
- net /cpu_hat/limit_sw_under_fork_in: track 0.00 -> 38.2 mm, vias 0 -> 1
- net /cpu_hat/IN_B_fork_out: track 0.00 -> 37.9 mm, vias 0 -> 1
- net /cpu_hat/limit_sw_upper_arm_in: track 0.00 -> 34.6 mm, vias 0 -> 2
- net Net-(J17-Pin_1): track 0.00 -> 33.8 mm
- net /cpu_hat/servo_2_out: track 0.00 -> 33.6 mm
- net /cpu_hat/limit_sw_under_arm_in: track 0.00 -> 33.6 mm, vias 0 -> 2
- net /cpu_hat/servo_3_out: track 0.00 -> 33.2 mm
- net Net-(J17-Pin_3): track 0.00 -> 32.3 mm
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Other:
- board size 123.1 x 120.2 mm -> 211 x 99 mm

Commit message: most of wire placed. try update kicad to use replicate library
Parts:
- removed J27: servo_0, Connector_PinHeader_2.54mm:PinHeader_1x03_P2.54mm_Vertical
- removed J28: servo_1, Connector_PinHeader_2.54mm:PinHeader_1x03_P2.54mm_Vertical
- removed J29: servo_2, Connector_PinHeader_2.54mm:PinHeader_1x03_P2.54mm_Vertical
- removed J30: servo_3, Connector_PinHeader_2.54mm:PinHeader_1x03_P2.54mm_Vertical
- added H25: Hole_arm, MountingHole:MountingHole_3.2mm_M3, F.Cu at (187.5, 75.2)
- added H26: Hole_arm, MountingHole:MountingHole_3.2mm_M3, F.Cu at (187.5, 98.2)
- added J55: servo connectors, Conn:PinHeader_03x04_P2.54mm_Vertical, B.Cu at (200.5, 90.5)
- C10, C11, C12, C9, Q3, R27, R28, R33, R35, R40, R43, R46, R49, U11, U17, U22: moved to B.Cu
- moved J36 155.4 mm to (205.2, 95.8), turned to -90 degrees
- moved R27 141.4 mm to (173.8, 97.0), turned to 180 degrees
- moved R28 141.1 mm to (173.8, 99.3)
- moved R45 137.1 mm to (181.6, 92.6), turned to 90 degrees
- moved R44 134.2 mm to (192.8, 88.5), turned to -90 degrees
- moved R46 132.9 mm to (181.6, 90.8), turned to 90 degrees
- moved R26 132.9 mm to (206.1, 87.0), turned to 180 degrees
- moved D4 131.5 mm to (172.1, 97.0)
- moved D5 131.2 mm to (172.0, 99.3)
- moved R50 130.8 mm to (192.8, 92.6), turned to -90 degrees
- moved R29 129.8 mm to (206.1, 91.4)
- moved R33 129.4 mm to (181.6, 83.0), turned to 90 degrees
- moved R36 127.7 mm to (192.8, 84.7), turned to -90 degrees
- moved Q3 126.0 mm to (189.2, 84.6)
- moved R30 124.7 mm to (206.0, 88.9), turned to 180 degrees
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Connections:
- net /cpu/emerg_detector renamed /cpu/emerge_detector
- net emerge_detector renamed emerge_detector_out
- J10 pad 16: power_checker -> power_checker_out
- J10 pad 18: emerge_order -> emerge_order_in
- J23 pad 6: +3V3 -> Vin_3V3_cpu_hat
- J24 pad 6: +3V3 -> Vin_3V3_cpu_hat
- J25 pad 6: +3V3 -> Vin_3V3_cpu_hat
- J31 pad 1: +3V3 -> Vin_3V3_cpu_hat
- J32 pad 1: +3V3 -> Vin_3V3_cpu_hat
- J34 pad 3: emerge_order -> /cpu/emerge_order
- J34 pad 5: power_checker -> /cpu/power_checker
- J35 pad 19: +3V3 -> Vin_3V3_cpu_hat
- J35 pad 2: +5V -> Vin_cpu_hat
- J38 pad 6: Vin_cpu -> Vin_arm
- J39 pad 1: GND1 -> /GND_md_1
- J39 pad 6: Vin_cpu -> Vin_md
- J40 pad 1: GND1 -> /GND_md
- J40 pad 6: Vin_cpu -> Vin_md
- J41 pad 2: +3V3 -> Vin_3V3_cpu_hat
- J41 pad 3: +5V -> Vin_cpu_hat
- J42 pad 4: +5V -> Vin_cpu_hat
- J46 pad 2: +3V3 -> Vin_3V3_cpu_hat
- J47 pad 2: +5V -> Vin_cpu_hat
- J53 pad 1: +5V -> Vin_cpu_hat
- J53 pad 2: +3V3 -> Vin_3V3_cpu_hat
- J54 pad 1: +5V -> Vin_cpu_hat
- J54 pad 2: +3V3 -> Vin_3V3_cpu_hat
- J59 pad 16: GND1 -> Vin_cpu_hat
- J59 pad 2: +3V3 -> Vin_3V3_cpu_hat
- J60 pad 16: GND1 -> Vin_cpu_hat
- J60 pad 2: +3V3 -> Vin_3V3_cpu_hat
- R14 pad 2: Vin_cpu -> Vin_md
- R15 pad 2: Vin_cpu -> Vin_md
- R17 pad 2: Vin_cpu -> Vin_md
- R20 pad 2: Vin_cpu -> Vin_md
- R22 pad 1: Vin_cpu -> Vin_md
- R23 pad 1: Vin_cpu -> Vin_md
- R24 pad 1: Vin_cpu -> Vin_md
- R25 pad 1: Vin_cpu -> Vin_md
- R30 pad 2: Vin_cpu -> Vin_arm
- R32 pad 1: /arm/servo_0 -> /arm/servo_1
- R33 pad 2: Vin_cpu -> Vin_arm
- R37 pad 1: +3V3 -> +3V3_cpu
- R38 pad 1: +3V3 -> +3V3_cpu
- R39 pad 1: /arm/servo_1 -> /arm/servo_0
- R40 pad 2: Vin_cpu -> Vin_arm
- R43 pad 2: Vin_cpu -> Vin_arm
- R46 pad 2: Vin_cpu -> Vin_arm
- R51 pad 1: power_checker -> /cpu/power_checker
- R55 pad 1: emerge_order -> emerge_order_in
- U18 pad 3: power_checker -> power_checker_out
- U2 pad 19: /cpu/LED12 -> unconnected-(U2-LED12-Pad19)
- U2 pad 20: /cpu/LED13 -> unconnected-(U2-LED13-Pad20)
- U2 pad 21: /cpu/LED14 -> unconnected-(U2-LED14-Pad21)
- U2 pad 22: /cpu/LED15 -> unconnected-(U2-LED15-Pad22)
- U20 pad 3: emerge_order -> /cpu/emerge_order
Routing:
- net +3V3: track 136.1 -> 415.6 mm, vias 6 -> 39
- net +3V3_motor: track 0.00 -> 159.3 mm, vias 0 -> 16
- net +6V: track 44.6 -> 180.8 mm, vias 1 -> 3
- net +5V: track 59.2 -> 187.4 mm, vias 2 -> 8
- net Vin_cpu_hat: track 0.00 -> 121.5 mm, vias 0 -> 5
- net /cpu/GPIO17: track 0.00 -> 99.9 mm, vias 0 -> 2
- net /cpu/GPIO18: track 0.00 -> 99.2 mm, vias 0 -> 4
- net /cpu/SCL_cpu: track 0.00 -> 82.7 mm
- net /cpu/SDA_cpu: track 0.00 -> 81.1 mm, vias 0 -> 1
- net /cpu/LED10: track 0.00 -> 73.8 mm, vias 0 -> 6
- net /cpu/emerge_order: track 0.00 -> 72.6 mm, vias 0 -> 7
- net /cpu/LED9: track 0.00 -> 70.9 mm, vias 0 -> 7
- net /cpu/emerge_detector: track 0.00 -> 69.2 mm, vias 0 -> 9
- net /cpu/LED4: track 0.00 -> 67.8 mm, vias 0 -> 1
- net /cpu/LED8: track 0.00 -> 67.6 mm, vias 0 -> 1
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- added copper zone on B.Cu, net +5V
- added copper zone on F.Cu, net +5V
- added copper zone on B.Cu, net +6V_in
- added copper zone on F.Cu, net +6V_in
- added copper zone on B.Cu, net +6V_out
- added copper zone on F.Cu, net +6V_out
- added copper zone on B.Cu, net /cpu_hat/GND_usb
- added copper zone on F.Cu, net /cpu_hat/GND_usb
- added copper zone on B.Cu, net /external_io/GND_led
- added copper zone on F.Cu, net /external_io/GND_led
- added copper zone on B.Cu, net /external_io/GND_reset
- added copper zone on F.Cu, net /external_io/GND_reset
- added copper zone on B.Cu, net /external_io/GND_uart
- added copper zone on F.Cu, net /external_io/GND_uart
- added copper zone on B.Cu, net /external_io/GND_usb
- added copper zone on F.Cu, net /external_io/GND_usb
- added copper zone on B.Cu, net Net-(J1-Pin_1)
- added copper zone on F.Cu, net Net-(J1-Pin_1)
- added copper zone on B.Cu, net Net-(J1-Pin_2)
- added copper zone on F.Cu, net Net-(J1-Pin_2)
- added copper zone on B.Cu, net Net-(J2-Pin_1)
- added copper zone on F.Cu, net Net-(J2-Pin_1)
- added copper zone on B.Cu, net Net-(J2-Pin_2)
- added copper zone on F.Cu, net Net-(J2-Pin_2)
- added copper zone on F.Cu, net Net-(U2-A0)
